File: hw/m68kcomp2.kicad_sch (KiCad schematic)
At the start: 21 parts, among them U1 mc68030rc

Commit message: BERR watchdog
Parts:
- added C1: 0.1uF, Capacitor_SMD:C_0805_2012Metric_Pad1.18x1.45mm_HandSolder, symbol Device:C
- added U1: GAL16V8, Package_DIP:DIP-20_W7.62mm_Socket, symbol Logic_Programmable:GAL16V8
- added U2: 74HC393, Package_SO:SO-14_3.9x8.65mm_P1.27mm, symbol 74xx:74LS393
- added unit 2 of U3
- added X1: 25.175MHz, Oscillator:Oscillator_DIP-8, symbol Oscillator:CXO_DIP8
- C2, C3: renamed from C?; footprint (none) -> Capacitor_SMD:C_0805_2012Metric_Pad1.18x1.45mm_HandSolder
- R1: renamed from R?; footprint (none) -> OptoDevice:R_LDR_D13.8mm_P9.0mm_Vertical
- U11: renamed from U?; footprint (none) -> Package_DIP:DIP-40_W15.24mm_Socket
- U13, U14, U15: renamed from U?; footprint (none) -> Package_SO:SO-14_3.9x8.65mm_P1.27mm
- U17, U18: renamed from U?; footprint (none) -> Connector_Dsub:DSUB-9_Male_Horizontal_P2.77x2.54mm_EdgePinOffset9.40mm
- U3: renamed from U?; value 74LS10 -> 74HC10; footprint (none) -> Package_SO:SO-14_3.9x8.65mm_P1.27mm
- U4: renamed from U?; value 74LS148 -> 74HC148; footprint (none) -> Package_SO:SO-16_3.9x9.9mm_P1.27mm
- U6: renamed from U?; footprint (none) -> Package_DIP:DIP-28_W15.24mm_Socket
- U9: renamed from U?; footprint (none) -> Package_DIP:DIP-20_W7.62mm_Socket
- Y1: renamed from Y?; footprint (none) -> Crystal:Crystal_SMD_ECS_CSM3X-2Pin_7.6x4.1mm
- gave numbers to parts that had none: 6
- renumbered U1 to U5
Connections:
- net CPUCLK is gone; now on net CLK: U5.E1 (CLK)
- net FPUEN is gone; now on net ~{FPUEN}: U7.29 (~{CS})
- net D0: no longer U11.25 (D0)
- net D1: no longer U11.16 (D1)
- net D2: no longer U11.24 (D2)
- net D24: now also U11.25 (D0)
- net D25: now also U11.16 (D1)
- net D26: now also U11.24 (D2)
- net D27: now also U11.17 (D3)
- net D28: now also U11.23 (D4)
- net D29: now also U11.18 (D5)
- net D3: no longer U11.17 (D3)
- net D30: now also U11.22 (D6)
- net D31: now also U11.19 (D7)
- net D4: no longer U11.23 (D4)
- net D5: no longer U11.18 (D5)
- net D6: no longer U11.22 (D6)
- net D7: no longer U11.19 (D7)
- net GND: now also C1.2, U1.10 (GND), X1.4 (GND); no longer C3.2
- net VCC: now also C1.1, U1.20 (VCC), X1.8 (Vcc)
- net ~{AS}: now also U1.2 (I2)
- net ~{AVEC}: now also U1.5 (I5)
- net ~{DSACK0}: now also U1.3 (I3)
- net ~{DSACK1}: now also U1.4 (I4)
- net at U11.32 (X1/CLK), Y1.1: no longer C3.1
- net ~{FPUEN}: now reaches U9.18 (IO2)
- net CLK: now reaches U9.19 (IO1)
- net CLK: now also U1.1 (I1/CLK), X1.5 (OUT)
- net ~{BERR}: now reaches U5.H1 (~{BERR})
- net ~{BERR}: now also U3.6
- new net: U2.13 (CP), U2.6 (Q3)
- new net BERR: U2.9 (Q2), U3.3, U3.4, U3.5
- new net WDOG_RST: U1.14 (IO6), U2.12 (MR), U2.2 (MR)
- new net ~{WDOG_CNT}: U1.15 (IO5), U2.1 (CP)
- no-connect marks 19 -> 26
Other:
- note added: "decode.pld"
- note added: "glue.pld"
- note removed: "See decode.pld for logic equations and docs/design_notes for explanation"
- moved on the sheet: C2, R1, RN1, U10, U11, U12, U13, U14, U15, U16, U17, U18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

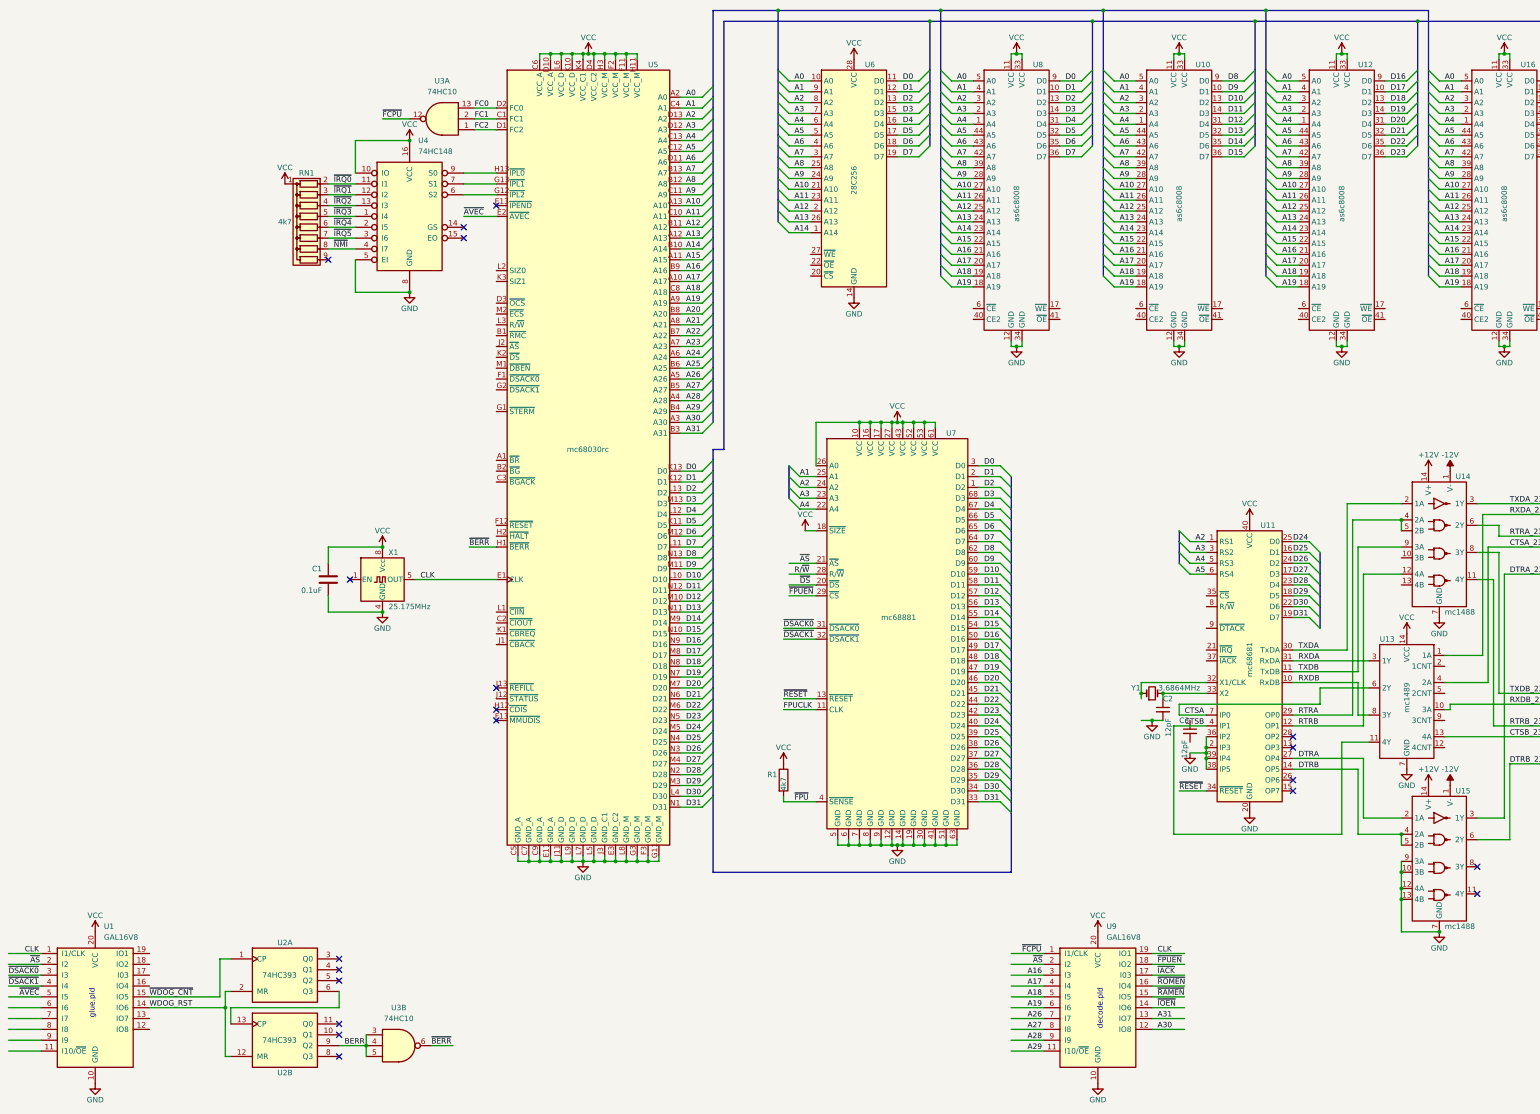
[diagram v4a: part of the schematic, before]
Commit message: simplified ram/rom dsack, reset watchdog on system reset, cache inhibit on I/O
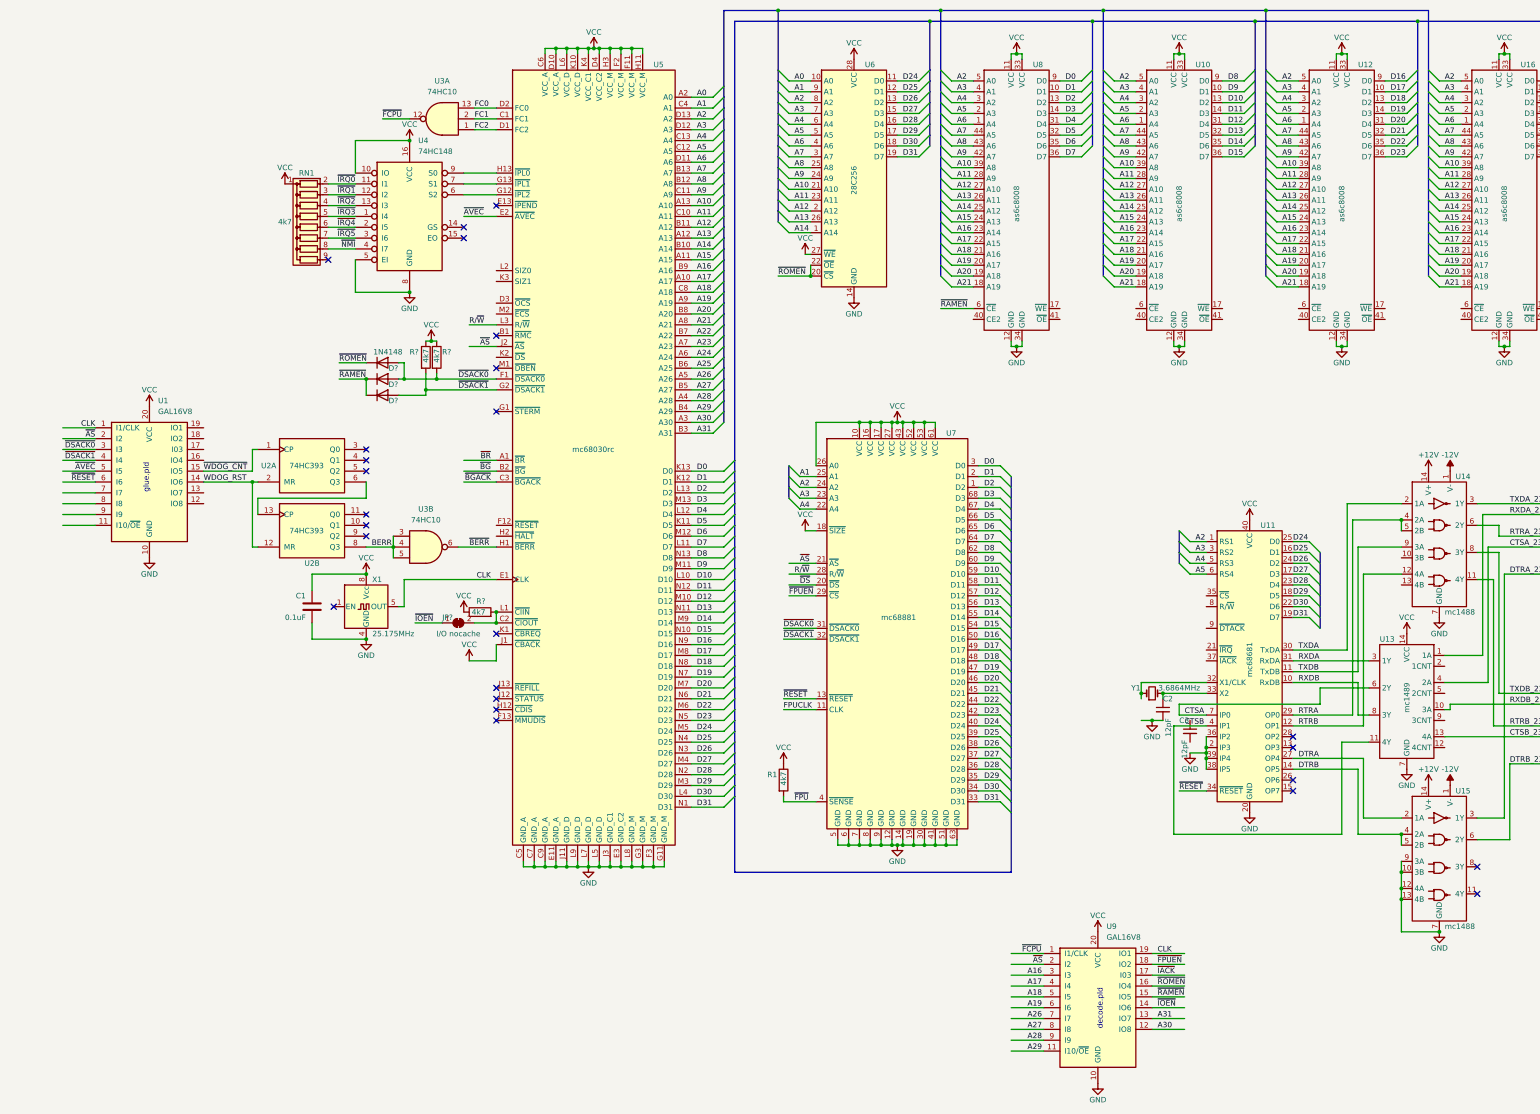
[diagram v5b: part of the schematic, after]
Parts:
- added D? (x3): 1N4148, Diode_THT:D_DO-35_SOD27_P7.62mm_Horizontal, symbol Diode:1N4148
- added JP?: I/O nocache, symbol Jumper:SolderJumper_2_Bridged
- added R? (x3): 4k7, OptoDevice:R_LDR_D13.8mm_P9.0mm_Vertical, symbol Device:R
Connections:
- net A0: no longer U10.5 (A0), U12.5 (A0), U16.5 (A0), U8.5 (A0)
- net A1: no longer U10.4 (A1), U12.4 (A1), U16.4 (A1), U8.4 (A1)
- net A10: now also U10.39 (A8), U12.39 (A8), U16.39 (A8), U8.39 (A8); no longer U10.27 (A10), U12.27 (A10), U16.27 (A10), U8.27 (A10)
- net A11: now also U10.28 (A9), U12.28 (A9), U16.28 (A9), U8.28 (A9); no longer U10.26 (A11), U12.26 (A11), U16.26 (A11), U8.26 (A11)
- net A12: now also U10.27 (A10), U12.27 (A10), U16.27 (A10), U8.27 (A10); no longer U10.25 (A12), U12.25 (A12), U16.25 (A12), U8.25 (A12)
- net A13: now also U10.26 (A11), U12.26 (A11), U16.26 (A11), U8.26 (A11); no longer U10.24 (A13), U12.24 (A13), U16.24 (A13), U8.24 (A13)
- net A14: now also U10.25 (A12), U12.25 (A12), U16.25 (A12), U8.25 (A12); no longer U10.23 (A14), U12.23 (A14), U16.23 (A14), U8.23 (A14)
- net A15: now also U10.24 (A13), U12.24 (A13), U16.24 (A13), U8.24 (A13); no longer U10.22 (A15), U12.22 (A15), U16.22 (A15), U8.22 (A15)
- net A16: now also U10.23 (A14), U12.23 (A14), U16.23 (A14), U8.23 (A14); no longer U10.21 (A16), U12.21 (A16), U16.21 (A16), U8.21 (A16)
- net A17: now also U10.22 (A15), U12.22 (A15), U16.22 (A15), U8.22 (A15); no longer U10.20 (A17), U12.20 (A17), U16.20 (A17), U8.20 (A17)
- net A18: now also U10.21 (A16), U12.21 (A16), U16.21 (A16), U8.21 (A16); no longer U10.19 (A18), U12.19 (A18), U16.19 (A18), U8.19 (A18)
- net A19: now also U10.20 (A17), U12.20 (A17), U16.20 (A17), U8.20 (A17); no longer U10.18 (A19), U12.18 (A19), U16.18 (A19), U8.18 (A19)
- net A2: now also U10.5 (A0), U12.5 (A0), U16.5 (A0), U8.5 (A0); no longer U10.3 (A2), U12.3 (A2), U16.3 (A2), U8.3 (A2)
- net A20: now also U10.19 (A18), U12.19 (A18), U16.19 (A18), U8.19 (A18)
- net A21: now also U10.18 (A19), U12.18 (A19), U16.18 (A19), U8.18 (A19)
- net A3: now also U10.4 (A1), U12.4 (A1), U16.4 (A1), U8.4 (A1); no longer U10.2 (A3), U12.2 (A3), U16.2 (A3), U8.2 (A3)
- net A4: now also U10.3 (A2), U12.3 (A2), U16.3 (A2), U8.3 (A2); no longer U10.1 (A4), U12.1 (A4), U16.1 (A4), U8.1 (A4)
- net A5: now also U10.2 (A3), U12.2 (A3), U16.2 (A3), U8.2 (A3); no longer U10.44 (A5), U12.44 (A5), U16.44 (A5), U8.44 (A5)
- net A6: now also U10.1 (A4), U12.1 (A4), U16.1 (A4), U8.1 (A4); no longer U10.43 (A6), U12.43 (A6), U16.43 (A6), U8.43 (A6)
- net A7: now also U10.44 (A5), U12.44 (A5), U16.44 (A5), U8.44 (A5); no longer U10.42 (A7), U12.42 (A7), U16.42 (A7), U8.42 (A7)
- net A8: now also U10.43 (A6), U12.43 (A6), U16.43 (A6), U8.43 (A6); no longer U10.39 (A8), U12.39 (A8), U16.39 (A8), U8.39 (A8)
- net A9: now also U10.42 (A7), U12.42 (A7), U16.42 (A7), U8.42 (A7); no longer U10.28 (A9), U12.28 (A9), U16.28 (A9), U8.28 (A9)
- net BERR: now also U2.8 (Q3); no longer U2.9 (Q2)
- net D0: no longer U6.11 (D0)
- net D1: no longer U6.12 (D1)
- net D2: no longer U6.13 (D2)
- net D24: now also U6.11 (D0)
- net D25: now also U6.12 (D1)
- net D26: now also U6.13 (D2)
- net D27: now also U6.15 (D3)
- net D28: now also U6.16 (D4)
- net D29: now also U6.17 (D5)
- net D3: no longer U6.15 (D3)
- net D30: now also U6.18 (D6)
- net D31: now also U6.19 (D7)
- net D4: no longer U6.16 (D4)
- net D5: no longer U6.17 (D5)
- net D6: no longer U6.18 (D6)
- net D7: no longer U6.19 (D7)
- net R/~{W}: now also U5.L3 (R/~{W})
- net VCC: now also U5.J1 (~{CBACK}), U6.27 (~{WE}), R?.1, R?.1, R?.1
- net ~{AS}: now also U5.J2 (~{AS})
- net ~{DSACK0}: now also U5.F1 (~{DSACK0}), D?.2 (A), D?.2 (A), R?.2
- net ~{DSACK1}: now also U5.G2 (~{DSACK1}), D?.2 (A), R?.2
- net ~{IOEN}: now also JP?.1 (A)
- net ~{RAMEN}: now also U8.6 (~{CE}), D?.1 (K), D?.1 (K)
- net ~{RESET}: now also U1.6 (I6)
- net ~{ROMEN}: now also U6.20 (~{CS}), U6.22 (~{OE}), D?.1 (K)
- net ~{BR}: now reaches U5.A1 (~{BR})
- net ~{BG}: now reaches U5.B2 (~{BG})
- net at U5.C2 (~{CIOUT}): now also U5.L1 (~{CIIN}), JP?.2 (B), R?.2
- net ~{BGACK}: now reaches U5.C3 (~{BGACK})
- no-connect marks 26 -> 31
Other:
- moved on the sheet: C1, U1, U2A, U2B, U3B, U5, X1

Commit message: progress
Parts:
- removed U1: GAL16V8, Package_DIP:DIP-20_W7.62mm_Socket, symbol Logic_Programmable:GAL16V8
- removed unit 2 of U3
- added C? (x2): 10uF, Capacitor_SMD:C_0805_2012Metric_Pad1.18x1.45mm_HandSolder, symbol Device:C_Small
- added R? (x2): 10k, symbol Device:R_Small
- added SW?: SWRST, symbol Switch:SW_Push
- added U?: GAL20V8, symbol m68kcomp2:GAL20V8
- added U? (x2): 74HC10, Package_SO:SO-14_3.9x8.65mm_P1.27mm, symbol 74xx:74LS10
- added U?: NE555D, Package_SO:SOIC-8_3.9x4.9mm_P1.27mm, symbol Timer:NE555D
- added U?: 74LS14, symbol 74xx:74LS14
- added U?: 74HC138, symbol 74xx:74LS138
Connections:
- net A1: now also U?.1 (A0)
- net A16: now also U?.7 (I7)
- net A17: now also U?.8 (I8)
- net A18: now also U?.9 (I9)
- net A19: now also U?.10 (I10)
- net A2: now also U?.2 (A1)
- net A20: now also U?.11 (I11)
- net A21: now also U?.13 (I13)
- net A22: now also U?.14 (I14)
- net A23: now also U?.15 (IO15)
- net A24: now also U?.16 (IO16)
- net A25: now also U?.17 (IO17)
- net A3: now also U?.3 (A2)
- net BERR: now also U?.3, U?.4, U?.5
- net CLK: now also U?.1 (I1)
- net GND: now also C3.2, C?.2, C?.2, SW?.1, U?.1 (GND), U?.12 (GND), U?.4 (E1), U?.8 (GND)
- net RTRB: now also U14.13 (4B)
- net R/~{W}: now also U10.17 (~{WE}), U11.8 (R/~{W}), U12.17 (~{WE}), U16.17 (~{WE}), U8.17 (~{WE}), U?.10, U?.11, U?.9
- net TXDB: now also U14.10 (3B)
- net VCC: now also U10.40 (CE2), U12.40 (CE2), U16.40 (CE2), U8.40 (CE2), R?.1, R?.2, U?.16 (VCC), U?.24 (VCC), U?.4 (R), U?.6 (E3), U?.8 (VCC)
- net WDOG_RST: now also U?.18 (IO18)
- net ~{AS}: now also U?.2 (I2)
- net ~{AVEC}: now also U?.5 (I5)
- net ~{BERR}: now also U?.6
- net ~{DSACK0}: now also U11.9 (~{DTACK}), U?.3 (I3)
- net ~{DSACK1}: now also U?.4 (I4)
- net ~{IACK}: now also U?.5 (E2)
- net ~{IOEN}: now also U?.23 (I23)
- net ~{IRQ0}: now also U11.21 (~{IRQ})
- net ~{RAMEN}: now also U10.6 (~{CE}), U12.6 (~{CE}), U16.6 (~{CE})
- net ~{RESET}: now also U5.F12 (~{RESET}), U?.2, U?.6 (I6)
- net ~{WDOG_CNT}: now also U?.19 (IO19)
- net at C3.1: now also U11.32 (X1/CLK), Y1.1
- net ~{RD}: now reaches U16.41 (~{OE})
- net ~{RD}: now also U10.41 (~{OE}), U12.41 (~{OE}), U8.41 (~{OE}), U?.8
- net ~{HALT}: now reaches U5.H2 (~{HALT})
- net ~{DUARTEN}: now reaches U11.35 (~{CS})
- net ~{DUARTEN}: now also U?.20 (I020)
- net ~{IACK0}: now reaches U11.37 (~{IACK})
- net ~{IACK0}: now also U?.14 (O1)
- new net: C?.1, R?.1, SW?.2, U?.2 (TR)
- new net: C?.1, R?.2, U?.6 (THR), U?.7 (DIS)
- new net RESET: U?.1, U?.3 (Q)
- new net ~{IACK1}: U?.13 (O2)
- new net ~{IACK2}: U?.12 (O3)
- new net ~{IACK3}: U?.11 (O4)
- new net ~{IACK4}: U?.10 (O5)
- new net ~{IACK5}: U?.9 (O6)
- no-connect marks 31 -> 38
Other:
- added sheet video (video.kicad_sch)
- moved on the sheet: C1, C2, C3, D?, JP?, R1, R?, RN1, U10, U11, U12, U13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

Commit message: schematic progress
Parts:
- added BT?: 3V, symbol Device:Battery_Cell
- added C? (x2): 12pF, Capacitor_SMD:C_0805_2012Metric_Pad1.18x1.45mm_HandSolder, symbol Device:C_Small
- added J?: SWRST, symbol Connector_Generic:Conn_01x02
- added U?: ds1501, symbol m68kcomp2:ds1501
- added Y?: 32.768kHz, Crystal:Crystal_SMD_ECS_CSM3X-2Pin_7.6x4.1mm, symbol Device:Crystal_Small
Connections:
- net A2: now also U?.10 (A0)
- net A3: now also U?.9 (A1)
- net A4: now also U?.8 (A2)
- net A5: now also U?.7 (A3)
- net A6: now also U?.6 (A4)
- net BERR: now also U?.6; no longer U2.8 (Q3), U?.3, U?.4, U?.5
- net D24: now also U?.11 (DQ0)
- net D25: now also U?.12 (DQ1)
- net D26: now also U?.13 (DQ2)
- net D27: now also U?.15 (DQ3)
- net D28: now also U?.16 (DQ4)
- net D29: now also U?.17 (DQ5)
- net D30: now also U?.18 (DQ6)
- net D31: now also U?.19 (DQ7)
- net GND: now also BT?.2 (-), C?.2, C?.2, J?.2 (Pin_2), U?.14 (GND), U?.21 (GND), U?.26 (VBAUX)
- net R/~{W}: now also U?.27 (~{WE})
- net VCC: now also R?.1, R?.2, U?.28 (VCC); no longer R?.1, R?.2
- net ~{BERR}: no longer U?.6
- net ~{RD}: now also U?.22 (~{OE})
- net at C?.1, SW?.2, U?.2 (TR): now also R?.2, J?.1 (Pin_1); no longer R?.1
- net at C?.1, U?.6 (THR), U?.7 (DIS): now also R?.1; no longer R?.2
- new net: C?.1, U?.2 (X1), Y?.2
- new net: BT?.1 (+), U?.25 (VBAT)
- new net: C?.1, U?.3 (X2), Y?.1
- new net: U2.8 (Q3), U?.3, U?.4, U?.5
- new net ~{RTCEN}: U?.20 (~{CE})
- no-connect marks 38 -> 47
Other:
- removed sheet video
- moved on the sheet: C1, C2, C3, C?, D?, JP?, R1, R?, RN1, SW?, U10, U11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

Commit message: avr handling SD card, keyboard, and mouse ports
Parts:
- added C?: 22uF, symbol Device:C_Polarized
- added C?: 10uF, symbol Device:C_Polarized
- added J?: AVR-ISP, symbol Connector:AVR-ISP-6
- added U? (x5): 74LVC125, symbol 74xx:74LVC125
- added U?: LM1117-3.3, symbol Regulator_Linear:LM1117-3.3
- added U?: mouse, symbol m68kcomp2:ps2conn
- added U?: kbd, symbol m68kcomp2:ps2conn
- added U?: sdcard, symbol m68kcomp2:sdcard
- added U?: ATmega328PB-A, Package_QFP:TQFP-32_7x7mm_P0.8mm, symbol MCU_Microchip_ATmega:ATmega328PB-A
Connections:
- net D24: now also U?.23 (PC0)
- net D25: now also U?.24 (PC1)
- net D26: now also U?.25 (PC2)
- net D27: now also U?.26 (PC3)
- net D28: now also U?.2 (PD4)
- net D29: now also U?.9 (PD5)
- net D30: now also U?.10 (PD6)
- net D31: now also U?.11 (PD7)
- net GND: now also C?.2, C?.2, J?.6 (GND), U?.1 (GND), U?.10 (SHELL), U?.21 (GND), U?.3 (GND), U?.3 (GND), U?.3 (VSS), U?.5 (GND), U?.6 (VSS), U?.7 (GND)
- net VCC: now also C?.1, J?.2 (VCC), U?.18 (AVCC), U?.3 (VI), U?.4 (VCC), U?.4 (VCC), U?.4 (VCC)
- net ~{RESET}: now also J?.5 (~{RST}), U?.29 (~{RESET}/PC6)
- net ~{IPL2}: now reaches U4.6 (S2), U5.G12 (~{IPL2})
- net ~{IPL1}: now reaches U4.7 (S1), U5.G13 (~{IPL1})
- net ~{IPL0}: now reaches U4.9 (S0), U5.H13 (~{IPL0})
- new net +3V3: C?.1, U?.14 (VCC), U?.2 (VO), U?.4 (VDD)
- new net KBCLK: U?.32 (PD2), U?.5 (CLK)
- new net KBDATA: U?.1 (DATA), U?.30 (PD0)
- new net MCLK: U?.1 (PD3), U?.5 (CLK)
- new net MDATA: U?.1 (DATA), U?.31 (PD1)
- new net MISO: J?.1 (MISO), U?.11, U?.16 (PB4)
- new net MOSI: J?.4 (MOSI), U?.14 (PB2), U?.15 (PB3), U?.2, U?.5
- new net SCK: J?.3 (SCK), U?.17 (PB5), U?.9
- new net SD_DI: U?.2 (CMD), U?.6
- new net SD_DO: U?.12, U?.7 (DAT0)
- new net SD_SCK: U?.5 (CLK), U?.8
- new net ~{SDBUFEN}: U?.1, U?.10, U?.13, U?.13 (PB1), U?.4
- new net ~{SD_CS_3V3}: U?.1 (CD/DAT3), U?.3
- no-connect marks 47 -> 48
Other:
- moved on the sheet: BT?, C2, C3, C?, U11, U13, U14, U15, U17, U18, U?, Y1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
